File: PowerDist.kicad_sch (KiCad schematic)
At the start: 0 parts

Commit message: sch is sching (tps2121 design)
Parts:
- added C2, C3, C4: 0.1u, symbol Device:C
- added C5: 1u, symbol Device:C
- added R4: 100k, symbol Device:R
- added R5, R8: 62k, symbol Device:R
- added R6, R7: 5k, symbol Device:R
- added U1: TPS2121RUXR, RUX0012A, symbol TPS2121:TPS2121RUXR
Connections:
- new net: R4.1, U1.10 (ILM)
- new net: C2.1, U1.11 (SS)
- new net: R5.2, R6.1, U1.4 (OV2)
- new net: R7.1, R8.2, U1.5 (OV1)
- new net +12V_CTRLS: C4.1, R5.1, U1.2 (IN2)
- new net +12V_EXT: C3.1, R8.1, U1.7 (IN1)
- new net +12V_SEL: C5.1, U1.1 (OUT), U1.8 (OUT)
- new net +12V_STATUS: U1.9 (ST)
- new net GND: C2.2, C3.2, C4.2, C5.2, R4.2, R6.2, R7.2, U1.12 (GND), U1.3 (CP2), U1.6 (PR1)
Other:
- sheet PowerProtection ports: added +12V_SEL; removed none
- note added: "RILM configured with minimum current limit of 1A (100kΩ)"
- note added: "Using VCOMP mode: - If only one input is valid, then that input will power the output - If both input voltages are equal, then IN2 (controls) takes priority For a source to be valid, it must be above UV (~2.6V) and below OV as defined by the OVx resistors From WaveSculptor 22 datasheet: "expects a DC supply on the CAN bus connection of between 9 and 15V" - Selected OV = ~14.2V"
- note added: "VREF = 1.06V = 14.204V * (5k/5k+62k)"

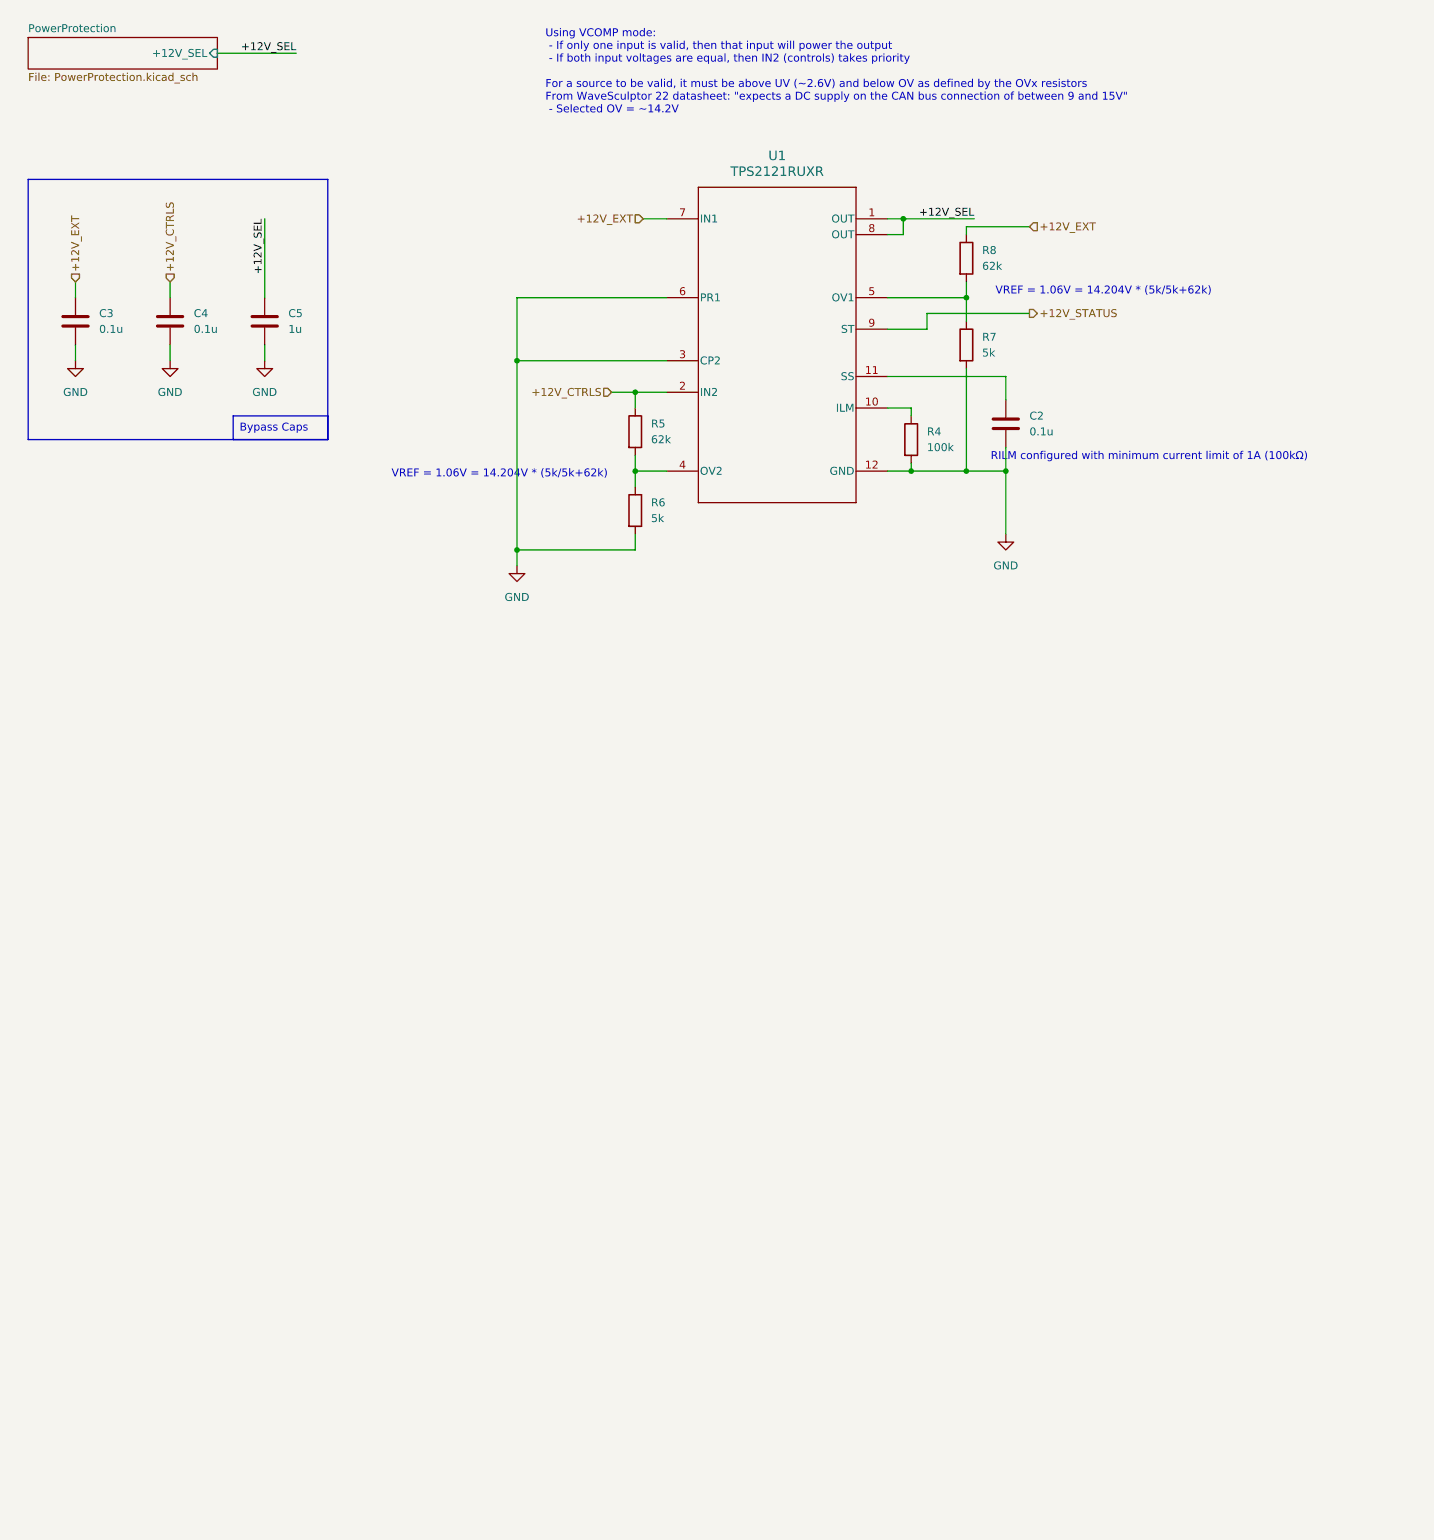
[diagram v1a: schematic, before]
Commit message: cleanup sch and add leds
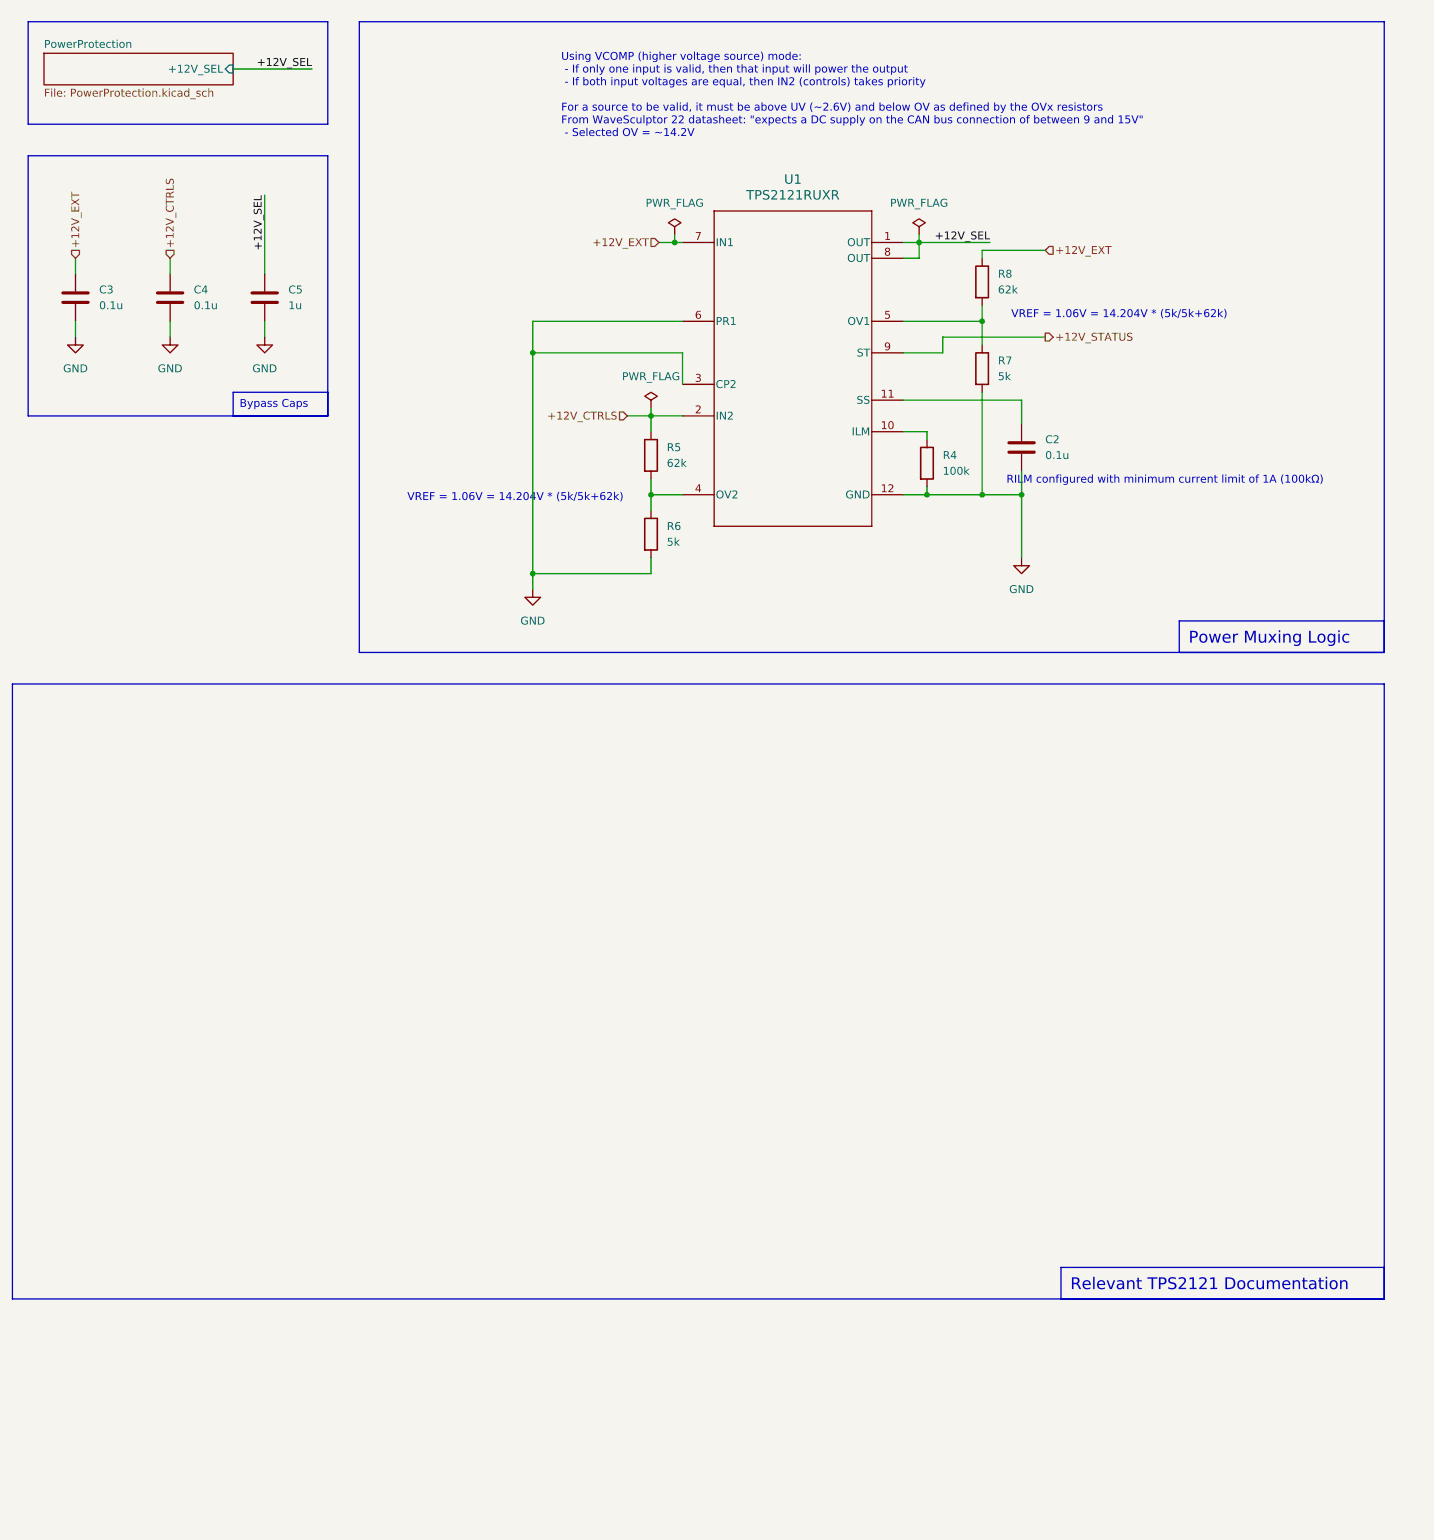
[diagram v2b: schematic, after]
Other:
- note added: "Using VCOMP (higher voltage source) mode: - If only one input is valid, then that input will power the output - If both input voltages are equal, then IN2 (controls) takes priority For a source to be valid, it must be above UV (~2.6V) and below OV as defined by the OVx resistors From WaveSculptor 22 datasheet: "expects a DC supply on the CAN bus connection of between 9 and 15V" - Selected OV = ~1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"
- note removed: "Using VCOMP mode: - If only one input is valid, then that input will power the output - If both input voltages are equal, then IN2 (controls) takes priority For a source to be valid, it must be above UV (~2.6V) and below OV as defined by the OVx resistors From WaveSculptor 22 datasheet: "expects a DC supply on the CAN bus connection of between 9 and 15V" - Selected OV = ~14.2V"
- moved on the sheet: C2, C3, C4, C5, R4, R5, R6, R7, R8, U1

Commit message: layout kinda screwy but it works?
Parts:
- added JP2: EXT ENABLE, Connector_PinHeader_2.54mm:PinHeader_1x02_P2.54mm_Vertical, symbol Jumper:Jumper_2_Open
- C2, C3, C4, C5: footprint (none) -> Capacitor_SMD:C_0805_2012Metric
- R4, R5, R6, R7, R8: footprint (none) -> Resistor_SMD:R_0805_2012Metric
- U1: footprint RUX0012A -> TPS2121:RUX0012A
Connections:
- net +12V_EXT: now also JP2.1 (A); no longer C3.1, R8.1, U1.7 (IN1)
- net ILM: now reaches R4.1, U1.10 (ILM)
- net CSS: now reaches C2.1, U1.11 (SS)
- net OV2: now reaches R5.2, R6.1, U1.4 (OV2)
- net OV1: now reaches R7.1, R8.2, U1.5 (OV1)
- new net +12V_EXT_EN: C3.1, JP2.2 (B), R8.1, U1.7 (IN1)
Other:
- note added: "Manual enable/disable for external pwr in case of issues with muxing IC"
- moved on the sheet: C3, C4, C5

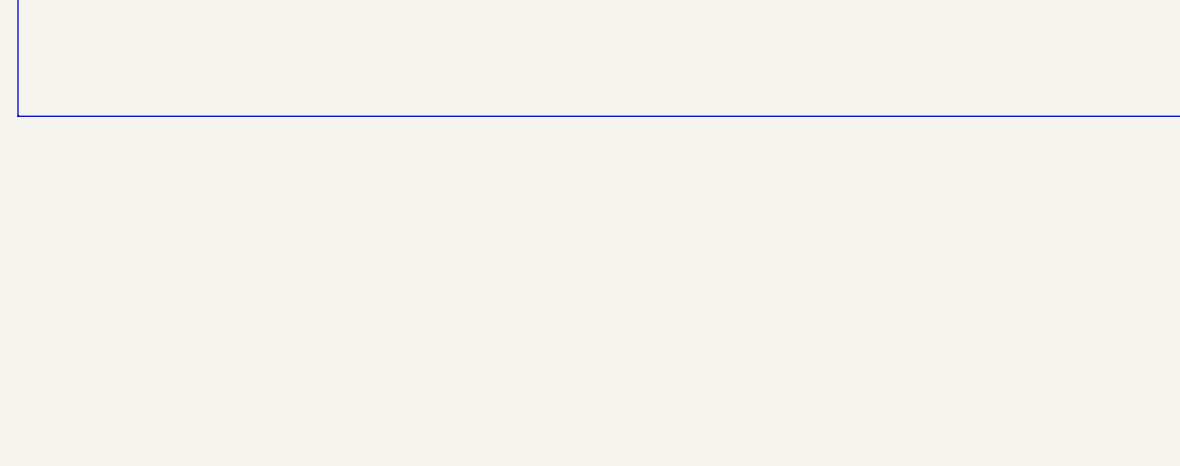
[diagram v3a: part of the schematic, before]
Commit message: better output/CAN routing + testpoints
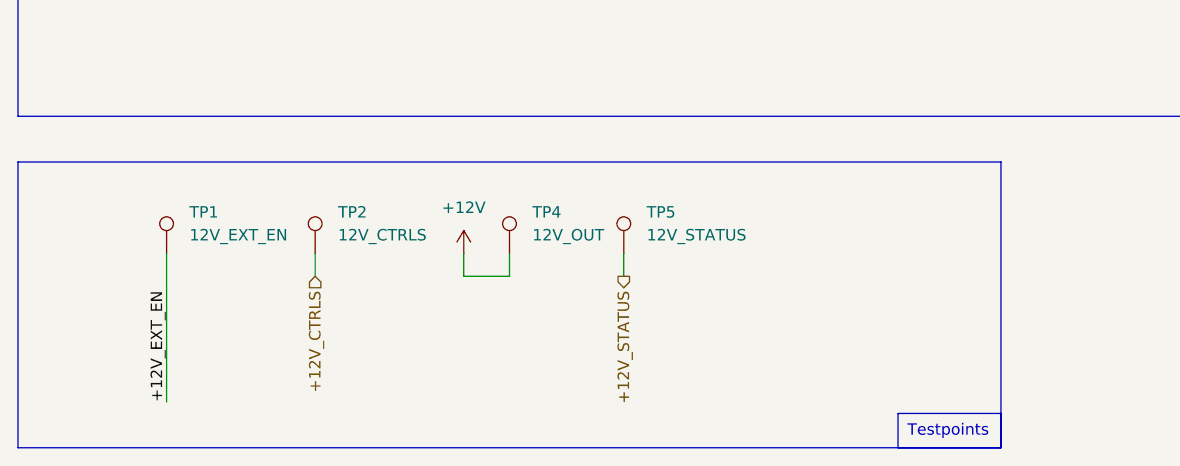
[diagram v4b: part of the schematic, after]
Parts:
- added TP1: 12V_EXT_EN, TestPoint:TestPoint_Pad_1.0x1.0mm, symbol Connector:TestPoint
- added TP2: 12V_CTRLS, TestPoint:TestPoint_Pad_1.0x1.0mm, symbol Connector:TestPoint
- added TP4: 12V_OUT, TestPoint:TestPoint_Pad_1.0x1.0mm, symbol Connector:TestPoint
- added TP5: 12V_STATUS, TestPoint:TestPoint_Pad_1.0x1.0mm, symbol Connector:TestPoint
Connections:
- net +12V_CTRLS: now also TP2.1
- net +12V_EXT_EN: now also TP1.1
- net +12V_STATUS: now also TP5.1
- new net +12V: TP4.1
